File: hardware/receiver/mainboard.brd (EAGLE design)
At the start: 47.3 x 38.1 mm, 16 parts, among them J2 POWER_JACKPTH, J3 AVR_SPI_PRG_6PTH, Q1 MOSFET-NCHANNELAO3404A, U1 ATMEGA328P_TQFP, U2 RFM69HCW

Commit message: Added BOM and diode protection
Receiver
* Added BOM
* Issue with relay activation voltage
 * Had to change VIN to 5V and add a regulator to 3.3B
 * Added VIN pin to expansion header
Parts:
- added D2: (no value), SparkFun-DiscreteSemi:SOD-323
- added R3: 47k, SparkFun-Passives:0603-RES
- added U3: (no value), SparkFun-PowerIC:TO-92
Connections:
- new net VIN: C4.1, D1.C, D2.C, J2.PWR, J5.2, U$1.5, U3.3
- net GND: now also J5.3, U3.2; no longer J5.2
- net N$1: now also R3.1
- net VCC: now also D2.A, R3.2, U3.1; no longer C4.1, D1.C, J2.PWR, U$1.5
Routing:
- net VCC: track 59.8 -> 34.1 mm
- net VIN: track 0.00 -> 10.2 mm
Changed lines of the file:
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@@
 <layers>
 <layer number="1" name="Top" color="4" fill="1" visible="yes" active="yes"/>
+<layer number="2" name="Route2" color="1" fill="3" visible="yes" active="yes"/>
+<layer number="3" name="Route3" color="4" fill="3" visible="yes" active="yes"/>
+<layer number="14" name="Route14" color="1" fill="6" visible="yes" active="yes"/>
+<layer number="15" name="Route15" color="4" fill="6" visible="yes" active="yes"/>
 <layer number="16" name="Bottom" color="1" fill="1" visible="yes" active="yes"/>
 <layer number="17" name="Pads" color="2" fill="1" visible="yes" active="yes"/>
@@
 </element>
 <element name="C4" library="SparkFun-Passives" package="1206" value="10u" x="44.3484" y="14.0208" rot="R270"/>
+<element name="R3" library="SparkFun-Passives" package="0603-RES" value="47k" x="0.6096" y="-2.5908"/>
+<element name="U3" library="SparkFun-PowerIC" package="TO-92" value="" x="1.8288" y="-7.3152"/>
+<element name="D2" library="SparkFun-DiscreteSemi" package="SOD-323" value="" x="-2.5908" y="-7.1628">
+<attribute name="PROD_ID" value="DIO-09646" x="-2.5908" y="-7.1628" size="1.778" layer="27" display="off"/>
+</element>
 </elements>
 <signals>
 <signal name="GND">
-<contactref element="J2" pad="GNDBREAK"/>
-<contactref element="C1" pad="2"/>
-<contactref element="J2" pad="GND"/>
 <contactref element="U1" pad="21"/>
 <contactref element="U1" pad="3"/>
@@
 <contactref element="Q1" pad="2"/>
 <contactref element="R2" pad="1"/>
-<contactref element="J5" pad="2"/>
 <contactref element="C4" pad="2"/>
+<contactref element="J2" pad="GNDBREAK"/>
+<contactref element="J2" pad="GND"/>
+<contactref element="U3" pad="2"/>
+<contactref element="C1" pad="2"/>
+<contactref element="J5" pad="3"/>
 <wire x1="39.64" y1="30.8" x2="39.79" y2="35.56" width="0" layer="19" extent="1-1"/>
 <wire x1="44.3484" y1="12.6208" x2="39.64" y2="30.8" width="0" layer="19" extent="1-1"/>
@@
 <wire x1="20.45" y1="27.94" x2="11.97" y2="28.32" width="0" layer="19" extent="1-1"/>
 <wire x1="25.52" y1="15.89" x2="14.37" y2="13.4874" width="0" layer="19" extent="1-1"/>
-<wire x1="2.54" y1="5.08" x2="13.97" y2="5.08" width="0" layer="19" extent="1-1"/>
+<wire x1="2.54" y1="7.62" x2="13.97" y2="5.08" width="0" layer="19" extent="1-1"/>
+<wire x1="1.8288" y1="-5.4102" x2="2.54" y2="7.62" width="0" layer="19" extent="1-1"/>
 </signal>
 <signal name="VCC">
-<contactref element="J2" pad="PWR"/>
-<contactref element="C1" pad="1"/>
 <contactref element="R1" pad="1"/>
 <contactref element="C2" pad="1"/>
@@
 <contactref element="C3" pad="1"/>
 <contactref element="J3" pad="2"/>
-<contactref element="U$1" pad="5"/>
 <contactref element="J5" pad="1"/>
-<wire x1="14.97" y1="33.02" x2="14.97" y2="30.62" width="0.4064" layer="1"/>
-<wire x1="14.97" y1="30.62" x2="17.65" y2="27.94" width="0.4064" layer="1"/>
-<wire x1="43.18" y1="19.05" x2="35.814" y2="19.05" width="0.4064" layer="1"/>
 <wire x1="35.814" y1="19.05" x2="35.5092" y2="19.05" width="0.4064" layer="1"/>
 <wire x1="35.5092" y1="19.05" x2="29.718" y2="24.8412" width="0.4064" layer="1"/>
 <wire x1="29.718" y1="24.8412" x2="20.7488" y2="24.8412" width="0.4064" layer="1"/>
-<wire x1="20.7488" y1="24.8412" x2="17.65" y2="27.94" width="0.4064" layer="1"/>
 <wire x1="44.3992" y1="9.1812" x2="44.3992" y2="9.2456" width="0.4064" layer="1"/>
-<contactref element="D1" pad="C"/>
-<wire x1="45.5676" y1="21.71" x2="45.5676" y2="21.4376" width="0.4064" layer="1"/>
-<wire x1="45.5676" y1="21.4376" x2="43.18" y2="19.05" width="0.4064" layer="1"/>
-<contactref element="C4" pad="1"/>
-<wire x1="44.3484" y1="15.4208" x2="44.3484" y2="17.8816" width="0.4064" layer="1"/>
-<wire x1="44.3484" y1="17.8816" x2="43.18" y2="19.05" width="0.4064" layer="1"/>
 <wire x1="40.536" y1="9.906" x2="38.2524" y2="9.906" width="0.4064" layer="1"/>
 <wire x1="38.2524" y1="9.906" x2="36.4236" y2="11.7348" width="0.4064" layer="1"/>
 <wire x1="36.4236" y1="11.7348" x2="36.4236" y2="18.4404" width="0.4064" layer="1"/>
 <wire x1="36.4236" y1="18.4404" x2="35.814" y2="19.05" width="0.4064" layer="1"/>
+<wire x1="44.3992" y1="9.2456" x2="43.18" y2="9.2456" width="0.4064" layer="1"/>
+<wire x1="43.18" y1="9.2456" x2="42.5196" y2="9.906" width="0.4064" layer="1"/>
+<wire x1="42.5196" y1="9.906" x2="40.536" y2="9.906" width="0.4064" layer="1"/>
+<wire x1="40.536" y1="9.906" x2="40.52" y2="9.89" width="0.4064" layer="1"/>
+<contactref element="R3" pad="2"/>
+<contactref element="U3" pad="1"/>
+<contactref element="C1" pad="1"/>
+<contactref element="D2" pad="A"/>
+<wire x1="17.65" y1="27.94" x2="20.7488" y2="24.8412" width="0" layer="19" extent="1-1"/>
 <wire x1="15.97" y1="22.0726" x2="20.7488" y2="24.8412" width="0" layer="19" extent="1-1"/>
 <wire x1="15.17" y1="13.4874" x2="15.97" y2="22.0726" width="0" layer="19" extent="1-1"/>
@@
 <wire x1="8.89" y1="5.08" x2="13.12" y2="7.62" width="0" layer="19" extent="1-1"/>
 <wire x1="2.54" y1="2.54" x2="8.89" y2="5.08" width="0" layer="19" extent="1-1"/>
-<wire x1="44.3992" y1="9.2456" x2="43.18" y2="9.2456" width="0.4064" layer="1"/>
-<wire x1="43.18" y1="9.2456" x2="42.5196" y2="9.906" width="0.4064" layer="1"/>
-<wire x1="42.5196" y1="9.906" x2="40.536" y2="9.906" width="0.4064" layer="1"/>
-<wire x1="40.536" y1="9.906" x2="40.52" y2="9.89" width="0.4064" layer="1"/>
+<wire x1="1.4596" y1="-2.5908" x2="2.54" y2="2.54" width="0" layer="19" extent="1-1"/>
+<wire x1="0.5588" y1="-7.3152" x2="1.4596" y2="-2.5908" width="0" layer="19" extent="1-1"/>
+<wire x1="-1.4408" y1="-7.1628" x2="0.5588" y2="-7.3152" width="0" layer="19" extent="1-1"/>
 </signal>
 <signal name="N$2">
@@
 <contactref element="U2" pad="5"/>
 <contactref element="U1" pad="2"/>
+<contactref element="R3" pad="1"/>
 <wire x1="11.97" y1="13.4874" x2="25.52" y2="7.89" width="0" layer="19" extent="1-1"/>
+<wire x1="-0.2404" y1="-2.5908" x2="11.97" y2="13.4874" width="0" layer="19" extent="1-1"/>
 </signal>
 <signal name="N$3">
@@
 <wire x1="2.54" y1="12.7" x2="9.6774" y2="14.98" width="0" layer="19" extent="1-1"/>
 </signal>
+<signal name="VIN">
+<contactref element="J2" pad="PWR"/>
+<contactref element="U3" pad="3"/>
+<wire x1="14.97" y1="33.02" x2="14.97" y2="30.62" width="0.4064" layer="1"/>
+<contactref element="U$1" pad="5"/>
+<contactref element="D1" pad="C"/>
+<contactref element="C4" pad="1"/>
+<wire x1="45.5676" y1="21.71" x2="45.5676" y2="21.4376" width="0.4064" layer="1"/>
+<wire x1="45.5676" y1="21.4376" x2="43.18" y2="19.05" width="0.4064" layer="1"/>
+<wire x1="44.3484" y1="15.4208" x2="44.3484" y2="17.8816" width="0.4064" layer="1"/>
+<wire x1="44.3484" y1="17.8816" x2="43.18" y2="19.05" width="0.4064" layer="1"/>
+<contactref element="D2" pad="C"/>
+<contactref element="J5" pad="2"/>
+<wire x1="14.97" y1="30.62" x2="43.18" y2="19.05" width="0" layer="19" extent="1-1"/>
+<wire x1="2.54" y1="5.08" x2="14.97" y2="30.62" width="0" layer="19" extent="1-1"/>
+<wire x1="3.0988" y1="-7.3152" x2="2.54" y2="5.08" width="0" layer="19" extent="1-1"/>
+<wire x1="-3.7408" y1="-7.1628" x2="3.0988" y2="-7.3152" width="0" layer="19" extent="1-1"/>
+</signal>
 </signals>

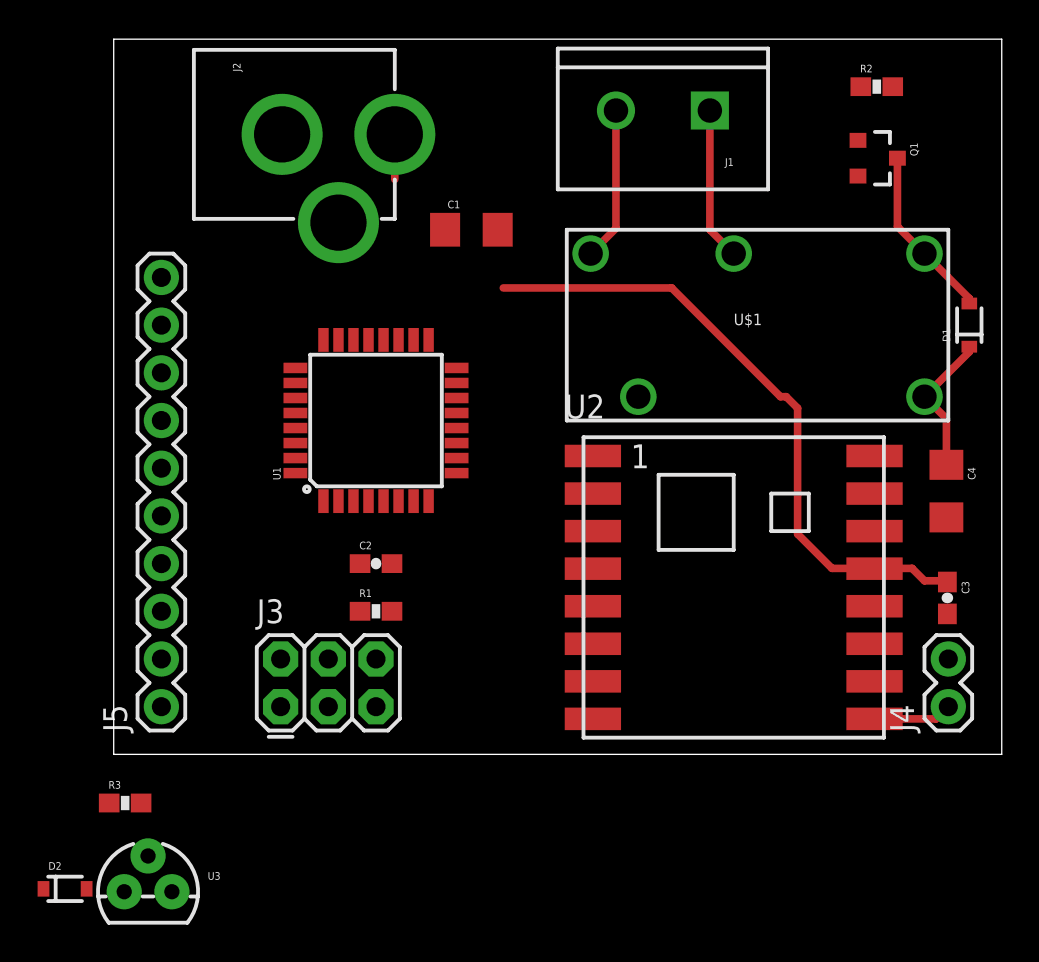
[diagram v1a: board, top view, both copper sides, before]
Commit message: Initial PCB layout of Receiver
Receiver
* Changed expansion connector pinout to make layout easier
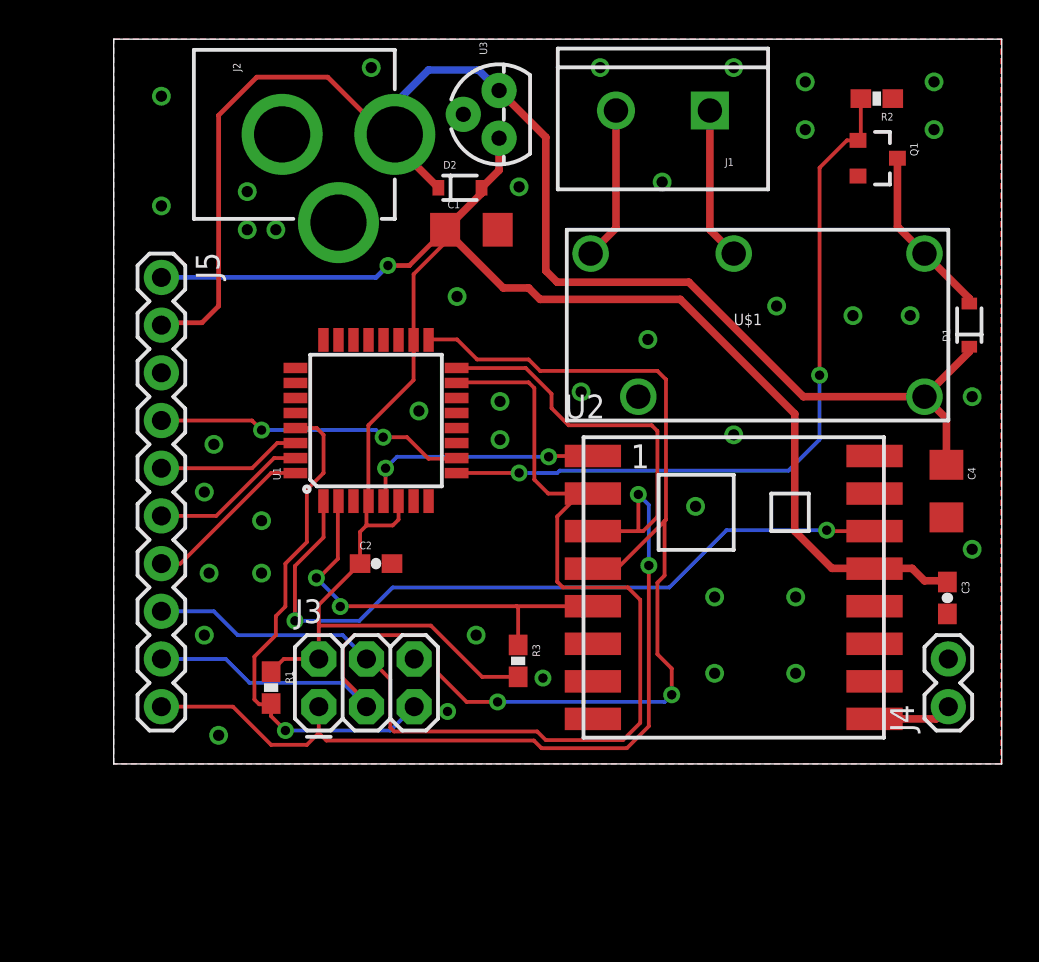
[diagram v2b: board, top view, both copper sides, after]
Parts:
- moved U3 45.4 mm to (20.5, 34.1), turned to 90 degrees
- moved D2 42.9 mm to (18.4, 30.2)
- moved J5 22.9 mm to (2.54, 25.4), turned to 270 degrees
- moved R3 22.3 mm to (21.5, 4.98), turned to 270 degrees
- moved R1 6.91 mm to (8.38, 3.56), turned to 270 degrees
- moved J3 2.03 mm to (10.9, 2.54)
- moved R2 0.64 mm to (40.6, 34.9), turned to 180 degrees
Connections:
- net MISO: now also J5.10; no longer J5.8
- net MOSI: now also J5.8; no longer J5.9
- net N$11: now also U1.30; no longer U1.32
- net N$9: now also U1.32; no longer U1.30
- net SCK: now also J5.9; no longer J5.10
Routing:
- net SCK: track 0.00 -> 71.6 mm, vias 0 -> 2
- net VCC: track 34.1 -> 103.3 mm, vias 0 -> 1
- net VIN: track 10.2 -> 78.9 mm
- net MISO: track 0.00 -> 64.7 mm, vias 0 -> 2
- net MOSI: track 0.00 -> 59.4 mm
- net N$3: track 0.00 -> 39.9 mm, vias 0 -> 2
- net N$8: track 0.00 -> 39.5 mm, vias 0 -> 2
- net N$2: track 0.00 -> 27.4 mm, vias 0 -> 1
- net N$1: track 0.00 -> 22.3 mm, vias 0 -> 2
- net N$12: track 0.00 -> 16.6 mm, vias 0 -> 2
- net GND: track 0.00 -> 13.1 mm, vias 0 -> 43
- net N$9: track 0.00 -> 9.14 mm
- net N$10: track 0.00 -> 8.41 mm
- net N$11: track 0.00 -> 7.69 mm
- added copper zone on layer 1, net GND
- added copper zone on layer 16, net GND
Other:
- board size 47.3 x 38.1 mm -> 47.3 x 38.6 mm

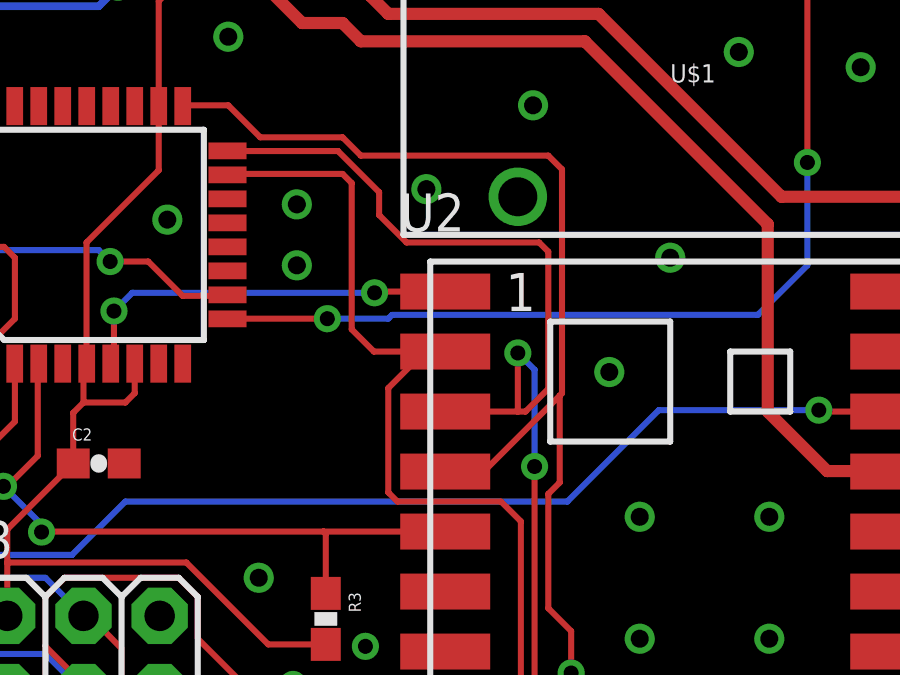
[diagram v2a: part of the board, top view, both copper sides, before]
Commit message: Fixed SPI mismatch
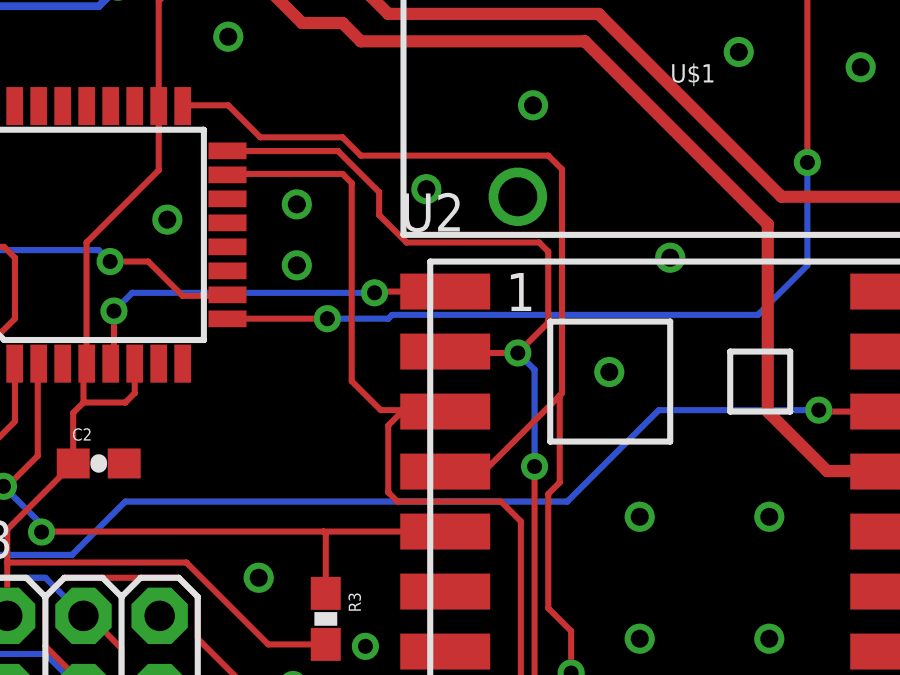
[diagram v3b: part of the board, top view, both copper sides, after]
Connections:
- net MISO: now also U2.2; no longer U2.3
- net MOSI: now also U2.3; no longer U2.2
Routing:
- net MISO: track 64.7 -> 60.6 mm
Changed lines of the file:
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@@
 <signal name="MOSI">
 <contactref element="J3" pad="4"/>
-<contactref element="U2" pad="2"/>
 <contactref element="U1" pad="15"/>
 <wire x1="22.4028" y1="19.5072" x2="22.098" y2="19.812" width="0.2032" layer="1"/>
 <wire x1="22.098" y1="19.812" x2="18.2946" y2="19.812" width="0.2032" layer="1"/>
 <wire x1="18.2946" y1="19.812" x2="18.2626" y2="19.78" width="0.2032" layer="1"/>
-<wire x1="25.52" y1="13.89" x2="24.8412" y2="13.89" width="0.2032" layer="1"/>
-<wire x1="24.8412" y1="13.89" x2="23.1432" y2="13.89" width="0.2032" layer="1"/>
-<wire x1="23.1432" y1="13.89" x2="22.4028" y2="14.6304" width="0.2032" layer="1"/>
-<wire x1="22.4028" y1="14.6304" x2="22.4028" y2="19.5072" width="0.2032" layer="1"/>
+<wire x1="22.4028" y1="12.9032" x2="22.4028" y2="19.5072" width="0.2032" layer="1"/>
 <wire x1="13.462" y1="5.08" x2="13.6652" y2="5.08" width="0.2032" layer="1"/>
 <wire x1="13.6652" y1="5.08" x2="14.732" y2="3.9878" width="0.2032" layer="1"/>
@@
 <wire x1="27.1272" y1="0.762" x2="28.0416" y2="1.6764" width="0.2032" layer="1"/>
 <wire x1="28.0416" y1="1.6764" x2="28.0416" y2="8.2296" width="0.2032" layer="1"/>
-<wire x1="23.622" y1="9.1948" x2="23.622" y2="12.6708" width="0.2032" layer="1"/>
-<wire x1="23.622" y1="12.6708" x2="24.8412" y2="13.89" width="0.2032" layer="1"/>
 <wire x1="23.622" y1="9.1948" x2="23.9268" y2="8.89" width="0.2032" layer="1"/>
 <wire x1="23.9268" y1="8.89" x2="27.3812" y2="8.89" width="0.2032" layer="1"/>
@@
 <wire x1="6.604" y1="6.35" x2="12.192" y2="6.35" width="0.2032" layer="16"/>
 <wire x1="12.192" y1="6.35" x2="13.462" y2="5.08" width="0.2032" layer="16"/>
+<contactref element="U2" pad="3"/>
+<wire x1="22.4028" y1="12.9032" x2="23.368" y2="11.938" width="0.2032" layer="1"/>
+<wire x1="23.368" y1="11.938" x2="24.13" y2="11.938" width="0.2032" layer="1"/>
+<wire x1="24.13" y1="11.938" x2="25.472" y2="11.938" width="0.2032" layer="1"/>
+<wire x1="25.472" y1="11.938" x2="25.52" y2="11.89" width="0.2032" layer="1"/>
+<wire x1="23.622" y1="9.1948" x2="23.622" y2="11.43" width="0.2032" layer="1"/>
+<wire x1="23.622" y1="11.43" x2="24.13" y2="11.938" width="0.2032" layer="1"/>
 </signal>
 <signal name="SCK">
@@
 <signal name="MISO">
 <contactref element="J3" pad="1"/>
-<contactref element="U2" pad="3"/>
 <contactref element="U1" pad="16"/>
-<wire x1="25.52" y1="11.89" x2="27.94" y2="11.89" width="0.2032" layer="1"/>
-<wire x1="27.94" y1="11.89" x2="28.1968" y2="11.89" width="0.2032" layer="1"/>
-<wire x1="28.1968" y1="11.89" x2="28.956" y2="12.6492" width="0.2032" layer="1"/>
-<wire x1="28.956" y1="12.6492" x2="28.956" y2="17.2212" width="0.2032" layer="1"/>
 <wire x1="28.956" y1="17.2212" x2="28.6512" y2="17.526" width="0.2032" layer="1"/>
 <wire x1="28.6512" y1="17.526" x2="24.2316" y2="17.526" width="0.2032" layer="1"/>
@@
 <wire x1="28.4988" y1="13.2842" x2="27.94" y2="13.843" width="0.2032" layer="16"/>
 <via x="27.94" y="13.843" extent="1-16" drill="0.5"/>
-<wire x1="27.94" y1="13.843" x2="27.94" y2="11.89" width="0.2032" layer="1"/>
 <contactref element="J5" pad="10"/>
 <wire x1="2.54" y1="2.54" x2="6.35" y2="2.54" width="0.2032" layer="1"/>
@@
 <wire x1="8.382" y1="0.508" x2="10.287" y2="0.508" width="0.2032" layer="1"/>
 <wire x1="10.287" y1="0.508" x2="10.922" y2="1.143" width="0.2032" layer="1"/>
+<contactref element="U2" pad="2"/>
+<wire x1="28.956" y1="17.2212" x2="28.956" y2="14.859" width="0.2032" layer="1"/>
+<wire x1="28.956" y1="14.859" x2="27.94" y2="13.843" width="0.2032" layer="1"/>
+<wire x1="27.94" y1="13.843" x2="25.567" y2="13.843" width="0.2032" layer="1"/>
+<wire x1="25.567" y1="13.843" x2="25.52" y2="13.89" width="0.2032" layer="1"/>
 </signal>
 <signal name="N$1">
